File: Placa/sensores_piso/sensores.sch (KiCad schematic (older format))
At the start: 4 parts

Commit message: trabajo en sensores
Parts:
- added K1: CONN_3, symbol CONN_3
- gave numbers to parts that had none: 2
- renumbered R_sens to R_sens1
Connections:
- net labels added: OUT, Vcc
- net labels removed: +5V
- wire segments 10 -> 12
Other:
- moved on the sheet: R_sens1
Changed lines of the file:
@@
-EESchema Schematic File Version 2  date Sun 14 Apr 2013 01:33:47 AM ART
+EESchema Schematic File Version 2  date mié 22 may 2013 20:07:39 ART
 LIBS:power
 LIBS:device
@@
 LIBS:contrib
 LIBS:valves
-EELAYER 43  0
+LIBS:cny70
+LIBS:sensores-cache
+LIBS:sensores-cache
+EELAYER 25  0
 EELAYER END
 $Descr A4 11700 8267
+encoding utf-8
 Sheet 1 1
 Title ""
-Date "14 apr 2013"
+Date "21 may 2013"
 Rev ""
 Comp ""
@@
 Comment4 ""
 $EndDescr
-Connection ~ 2750 1700
 Wire Wire Line
-	2750 1500 2750 2050
+	2950 1950 2950 1600
 Wire Wire Line
-	2750 1700 2600 1700
+	2750 2050 2750 1600
+Wire Wire Line
+	1950 1600 1950 2050
+Wire Wire Line
+	1950 1600 2100 1600
+Connection ~ 2850 2100
+Wire Wire Line
+	2850 1600 2850 2100
 Wire Wire Line
 	2750 2250 2750 2100
 Wire Wire Line
 	2750 2100 3000 2100
-Wire Wire Line
-	2100 1700 1950 1700
-Wire Wire Line
-	1950 1700 1950 2050
 Wire Wire Line
 	1950 2050 2050 2050
@@
 Wire Wire Line
 	3750 2450 3750 2250
+Wire Wire Line
+	2750 1600 2600 1600
+Text Label 2950 1600 3    60   ~ 0
+GND
+Text Label 2850 1600 3    60   ~ 0
+OUT
+Text Label 2750 1600 3    60   ~ 0
+Vcc
 $Comp
-L +5V #PWR?
-U 1 1 516A2BA2
-P 2750 1500
-F 0 "#PWR?" H 2750 1590 20  0001 C CNN
-F 1 "+5V" H 2750 1590 30  0000 C CNN
-	1    2750 1500
+L GND #PWR2
+U 1 1 519C08CF
+P 2950 1950
+F 0 "#PWR2" H 2950 1950 30  0001 C CNN
+F 1 "GND" H 2950 1880 30  0001 C CNN
+	1    2950 1950
 	1    0    0    -1
 $EndComp
 $Comp
-L GND #PWR?
+L CONN_3 K1
+U 1 1 519C0880
+P 2850 1250
+F 0 "K1" V 2800 1250 50  0000 C CNN
+F 1 "CONN_3" V 2900 1250 40  0000 C CNN
+	1    2850 1250
+	0    -1   -1   0
+$EndComp
+$Comp
+L GND #PWR3
 U 1 1 516A2B65
 P 3750 2450
-F 0 "#PWR?" H 3750 2450 30  0001 C CNN
+F 0 "#PWR3" H 3750 2450 30  0001 C CNN
 F 1 "GND" H 3750 2380 30  0001 C CNN
 	1    3750 2450
@@
 $EndComp
 $Comp
-L GND #PWR?
+L GND #PWR1
 U 1 1 516A2B56
 P 1950 2400
-F 0 "#PWR?" H 1950 2400 30  0001 C CNN
+F 0 "#PWR1" H 1950 2400 30  0001 C CNN
 F 1 "GND" H 1950 2330 30  0001 C CNN
 	1    1950 2400
@@
 $EndComp
 $Comp
-L POT RV?
+L POT RV1
 U 1 1 516A2B00
 P 3000 2250
-F 0 "RV?" H 3000 2150 50  0000 C CNN
+F 0 "RV1" H 3000 2150 50  0000 C CNN
 F 1 "POT" H 3000 2250 50  0000 C CNN
 	1    3000 2250
@@
 $EndComp
 $Comp
-L R R_sens
+L R R_sens1
 U 1 1 516A2AC6
-P 2350 1700
-F 0 "R_sens" V 2430 1700 50  0000 C CNN
-F 1 "200" V 2350 1700 50  0000 C CNN
-	1    2350 1700
+P 2350 1600
+F 0 "R_sens1" V 2430 1600 50  0000 C CNN
+F 1 "200" V 2350 1600 50  0000 C CNN
+	1    2350 1600
 	0    -1   -1   0
 $EndComp
 $Comp
-L CNY70 ???
+L CNY70 ??1
 U 1 1 516A2AAF
 P 2450 2150
-F 0 "???" H 2450 2150 60  0000 C CNN
+F 0 "??1" H 2450 2150 60  0000 C CNN
 F 1 "CNY70" H 2450 2150 60  0000 C CNN
 	1    2450 2150

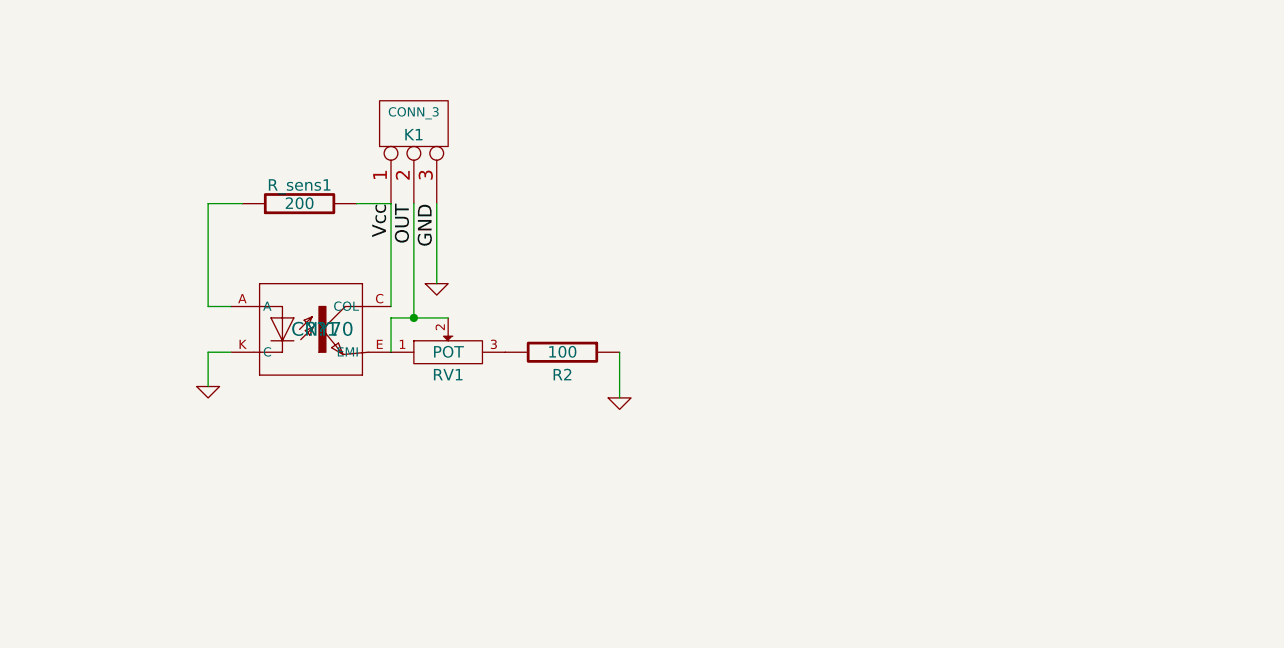
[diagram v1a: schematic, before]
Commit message: trabajo en Sensores de piso
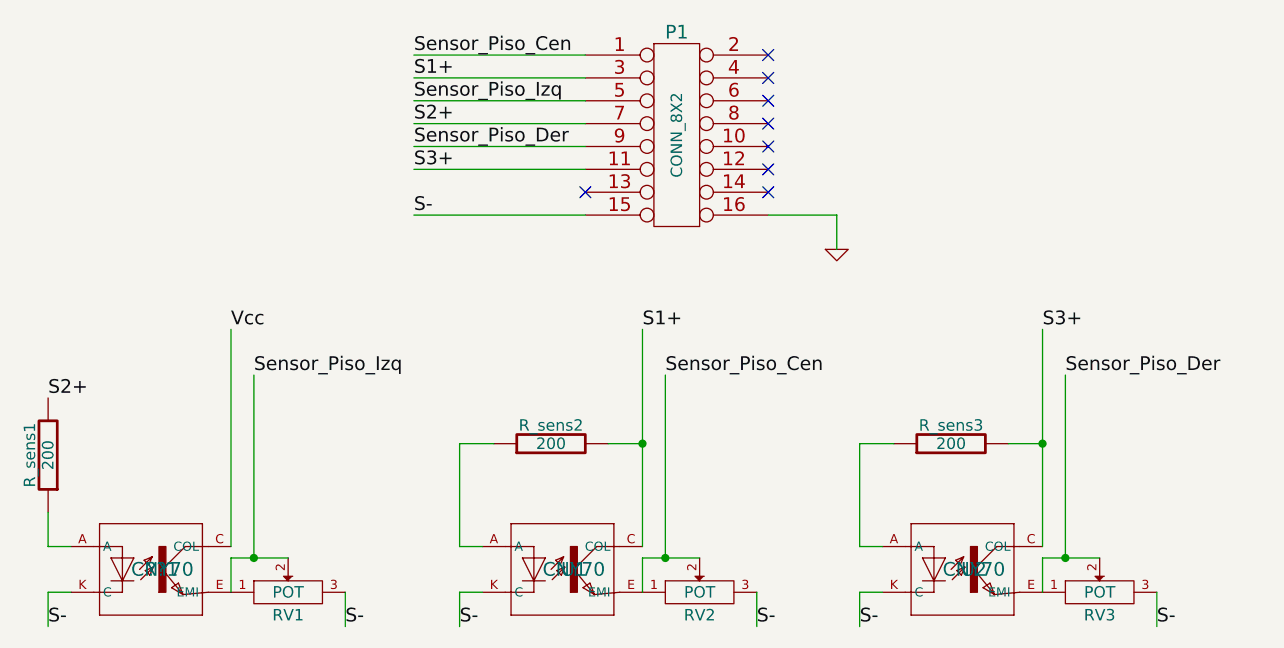
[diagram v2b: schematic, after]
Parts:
- removed K1: CONN_3, symbol CONN_3
- removed R2: 100, symbol R
- added P1: CONN_8X2, ~, symbol CONN_8X2
- added RV2, RV3: POT, symbol POT
- added R_sens2, R_sens3: 200, symbol R
- added U1, U2: CNY70, symbol CNY70
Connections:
- net GND: now also P1.16; no longer ??1.K (C)
- net Vcc: no longer R_sens1.2
- net S-: now reaches RV1.3
- net S-: now also ??1.K (C), P1.15, RV2.3, RV3.3, U1.K (C), U2.K (C)
- net OUT renamed Sensor_Piso_Izq
- net Sensor_Piso_Izq: now also P1.5
- new net: R_sens2.1, U1.A
- new net: R_sens3.1, U2.A
- new net S1+: P1.3, R_sens2.2, U1.C (COL)
- new net S2+: P1.7, R_sens1.2
- new net S3+: P1.11, R_sens3.2, U2.C (COL)
- new net Sensor_Piso_Cen: P1.1, RV2.1, RV2.2, U1.E (EMI)
- new net Sensor_Piso_Der: P1.9, RV3.1, RV3.2, U2.E (EMI)
- no-connect marks 0 -> 8
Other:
- moved on the sheet: ??1, RV1, R_sens1
